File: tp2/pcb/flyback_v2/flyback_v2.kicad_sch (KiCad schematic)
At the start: 57 parts, among them J1 Connector_2, J10 Connector_2, J11 Connector_2, J2 Connector_2, J3 Connector_2, J4 Connector_2, J5 Connector_2, J6 Connector_2, J7 Terminal_2, J8 Terminal_2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

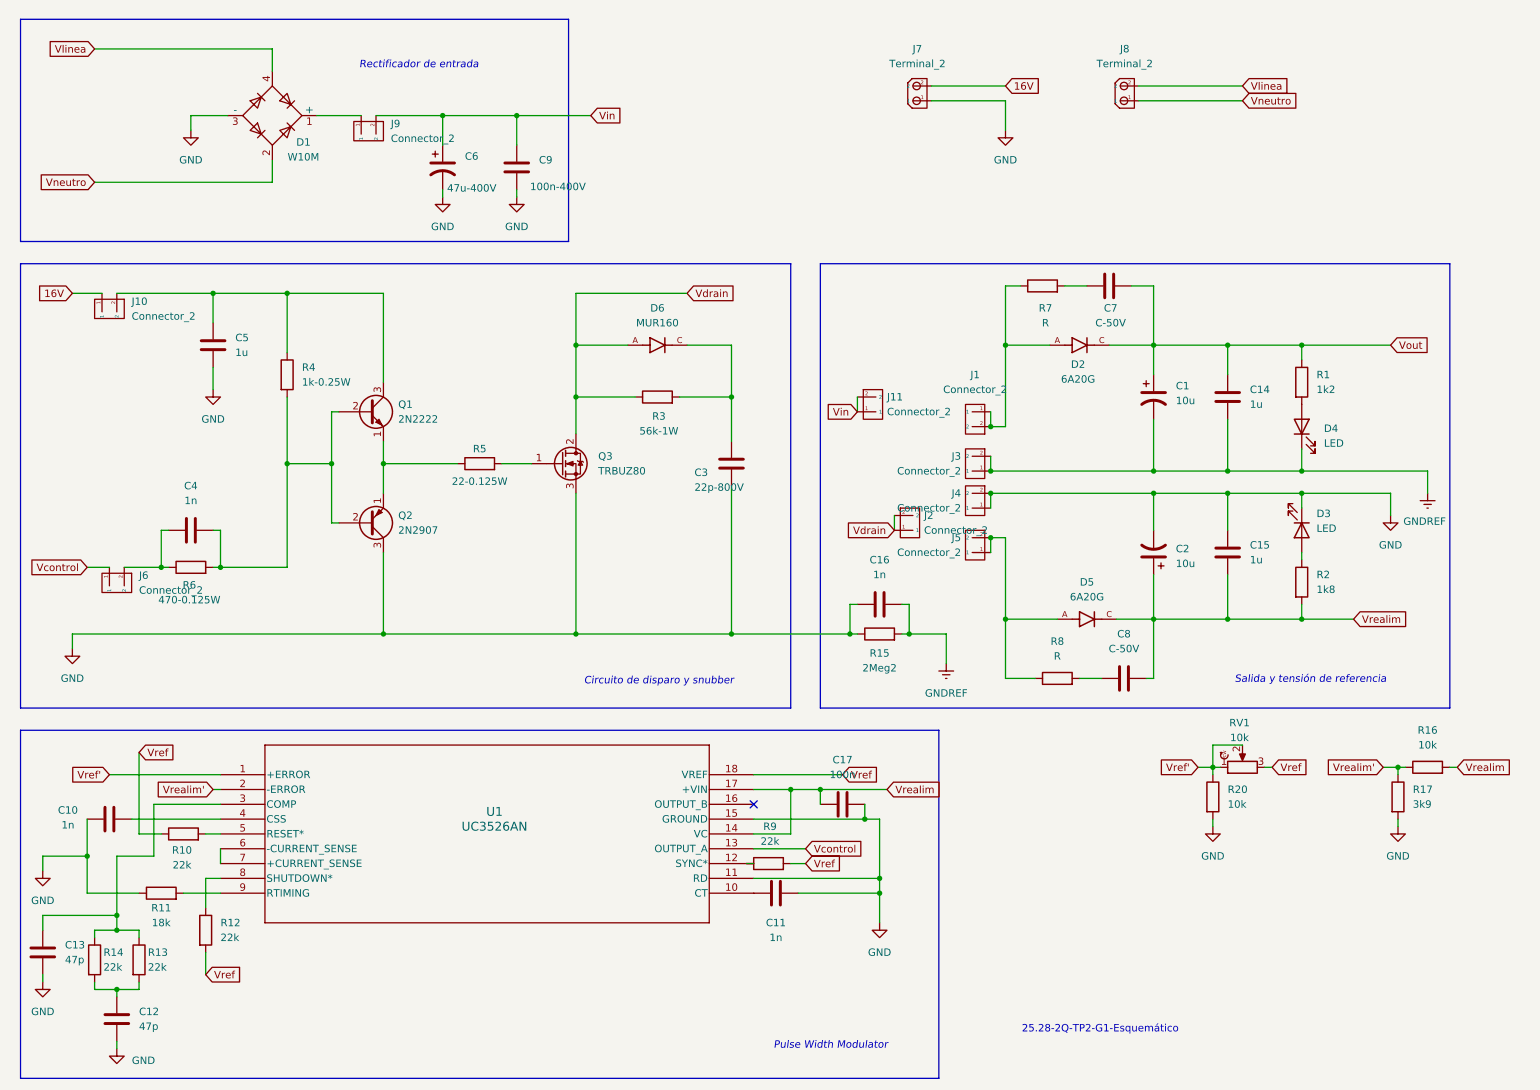
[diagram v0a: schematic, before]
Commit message: puse el jumper de Vrealim y 16V
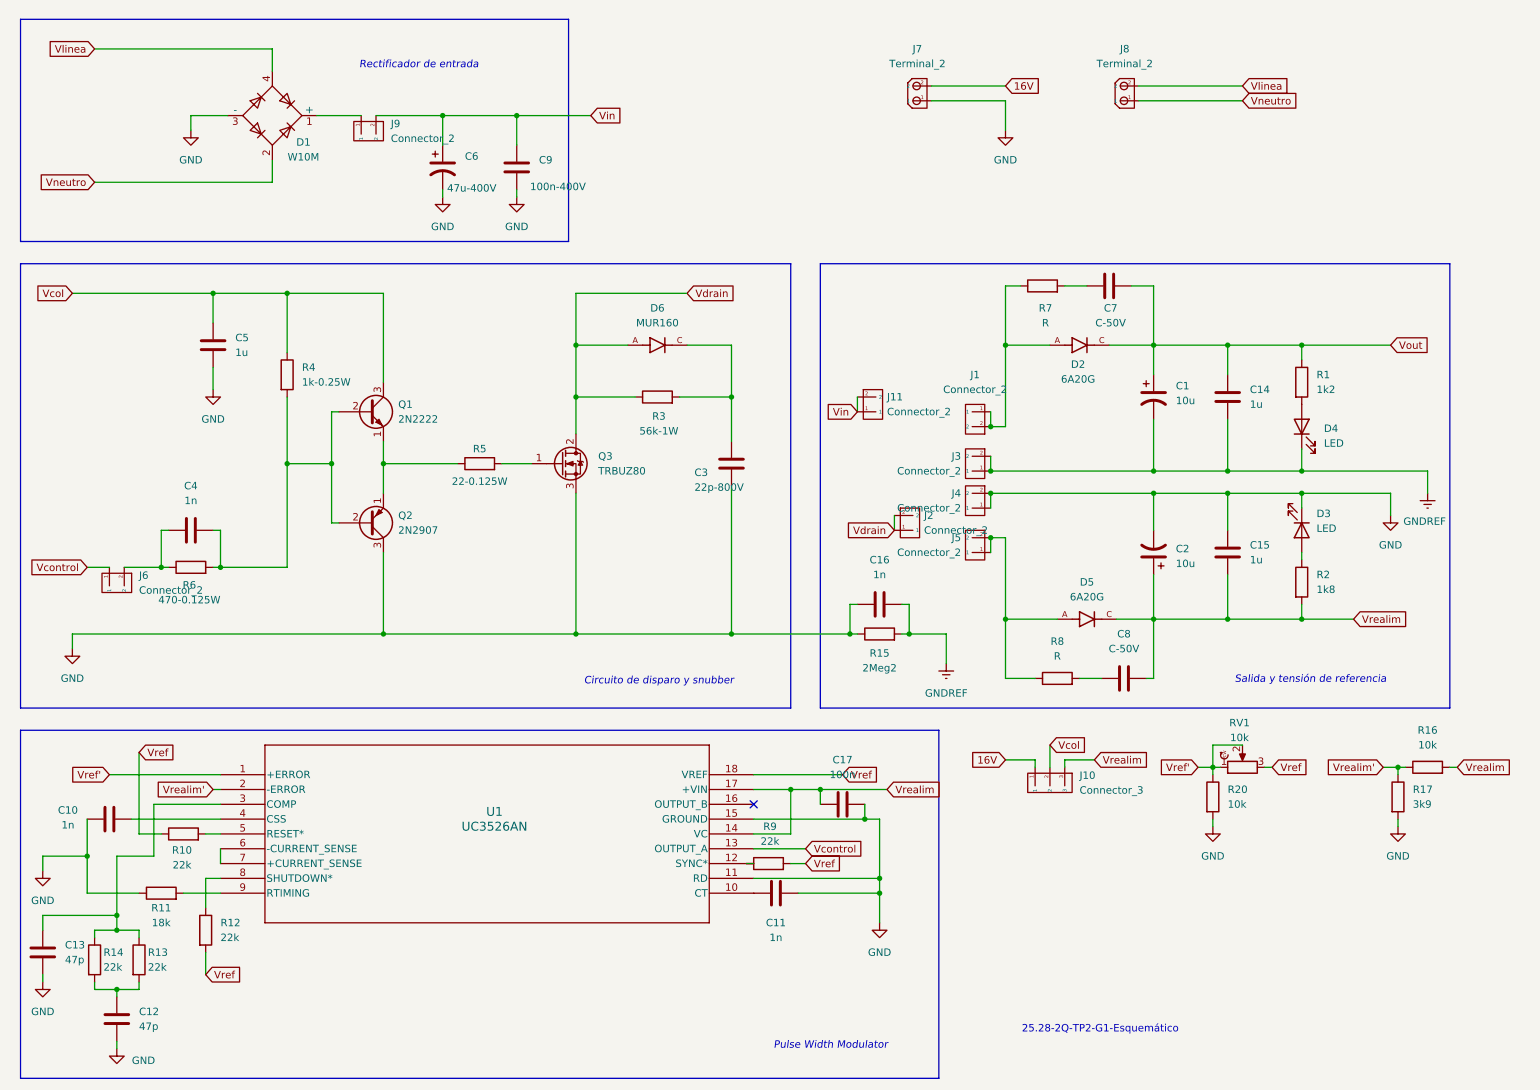
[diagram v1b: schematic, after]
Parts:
- removed J10: Connector_2, TCLib:PinHeader_1x02_P2.54mm_Vertical, symbol TCLib:Connector_2
- added J10: Connector_3, TCLib:PinHeader_1x03_P2.54mm_Vertical, symbol TCLib:Connector_3
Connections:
- net 16V: now also J10.1
- net Vrealim: now also J10.3
- net Vcol: now reaches C5.1, Q1.3 (C), R4.1
- net Vcol: now also J10.2
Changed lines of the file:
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@@
 	(wire
 		(pts
+			(xy 193.04 144.78) (xy 193.04 143.51)
+		)
+		(stroke
+			(width 0)
+			(type default)
+		)
+	)
+	(wire
+		(pts
 			(xy 187.96 105.41) (xy 187.96 119.38)
 		)
@@
 	(wire
 		(pts
+			(xy 198.12 143.51) (xy 203.2 143.51)
+		)
+		(stroke
+			(width 0)
+			(type default)
+		)
+	)
+	(wire
+		(pts
 			(xy 50.8 163.83) (xy 50.8 168.91)
 		)
@@
 	(wire
 		(pts
+			(xy 198.12 144.78) (xy 198.12 143.51)
+		)
+		(stroke
+			(width 0)
+			(type default)
+		)
+	)
+	(wire
+		(pts
 			(xy 91.44 33.02) (xy 104.14 33.02)
 		)
@@
 	(wire
 		(pts
-			(xy 35.56 63.5) (xy 52.07 63.5)
-		)
-		(stroke
-			(width 0)
-			(type default)
-		)
-	)
-	(wire
-		(pts
 			(xy 35.56 182.88) (xy 35.56 184.15)
 		)
@@
 	(wire
 		(pts
+			(xy 187.96 143.51) (xy 193.04 143.51)
+		)
+		(stroke
+			(width 0)
+			(type default)
+		)
+	)
+	(wire
+		(pts
 			(xy 252.73 144.78) (xy 255.27 144.78)
 		)
@@
 	(wire
 		(pts
+			(xy 195.58 140.97) (xy 195.58 144.78)
+		)
+		(stroke
+			(width 0)
+			(type default)
+		)
+	)
+	(wire
+		(pts
 			(xy 41.91 151.13) (xy 41.91 160.02)
 		)
@@
 	(wire
 		(pts
-			(xy 27.94 63.5) (xy 33.02 63.5)
+			(xy 27.94 63.5) (xy 52.07 63.5)
 		)
 		(stroke
@@
 		)
 	)
+	(global_label "Vrealim"
+		(shape input)
+		(at 203.2 143.51 0)
+		(fields_autoplaced yes)
+		(effects
+			(font
+				(size 1.27 1.27)
+			)
+			(justify left)
+		)
+		(property "Intersheetrefs" "${INTERSHEET_REFS}"
+			(at 213.2609 143.51 0)
+			(effects
+				(font
+					(size 1.27 1.27)
+				)
+				(justify left)
+				(hide yes)
+			)
+		)
+	)
 	(global_label "Vref"
 		(shape input)
@@
 	(global_label "16V"
 		(shape input)
+		(at 187.96 143.51 180)
+		(fields_autoplaced yes)
+		(effects
+			(font
+				(size 1.27 1.27)
+			)
+			(justify right)
+		)
+		(property "Intersheetrefs" "${INTERSHEET_REFS}"
+			(at 181.4672 143.51 0)
+			(effects
+				(font
+					(size 1.27 1.27)
+				)
+				(justify right)
+				(hide yes)
+			)
+		)
+	)
+	(global_label "16V"
+		(shape input)
 		(at 187.96 27.94 0)
 		(fields_autoplaced yes)
@@
 		)
 	)
+	(global_label "Vcol"
+		(shape input)
+		(at 195.58 140.97 0)
+		(fields_autoplaced yes)
+		(effects
+			(font
+				(size 1.27 1.27)
+			)
+			(justify left)
+		)
+		(property "Intersheetrefs" "${INTERSHEET_REFS}"
+			(at 202.5566 140.97 0)
+			(effects
+				(font
+					(size 1.27 1.27)
+				)
+				(justify left)
+				(hide yes)
+			)
+		)
+	)
 	(global_label "Vref"
 		(shape input)
@@
 		)
 	)
-	(global_label "16V"
+	(global_label "Vcol"
 		(shape input)
 		(at 27.94 63.5 180)
@@
 		)
 		(property "Intersheetrefs" "${INTERSHEET_REFS}"
-			(at 21.4472 63.5 0)
+			(at 20.9634 63.5 0)
 			(effects
 				(font
@@
 	)
 	(symbol
-		(lib_id "TCLib:Connector_2")
-		(at 34.29 66.04 270)
-		(unit 1)
-		(exclude_from_sim no)
-		(in_bom yes)
-		(on_board yes)
-		(dnp no)
-		(fields_autoplaced yes)
-		(property "Reference" "J10"
-			(at 38.1 64.8969 90)
-			(effects
-				(font
-					(size 1.27 1.27)
-				)
-				(justify left)
-			)
-		)
-		(property "Value" "Connector_2"
-			(at 38.1 67.4369 90)
-			(effects
-				(font
-					(size 1.27 1.27)
-				)
-				(justify left)
-			)
-		)
-		(property "Footprint" "TCLib:PinHeader_1x02_P2.54mm_Vertical"
-			(at 38.608 65.532 0)
-			(effects
-				(font
-					(size 1.27 1.27)
-				)
-				(hide yes)
-			)
-		)
-		(property "Datasheet" ""
-			(at 34.29 66.04 0)
-			(effects
-				(font
-					(size 1.27 1.27)
-				)
-				(hide yes)
-			)
-		)
-		(property "Description" ""
-			(at 34.29 66.04 0)
-			(effects
-				(font
-					(size 1.27 1.27)
-				)
-				(hide yes)
-			)
-		)
-		(pin "2"
-		)
-		(pin "1"
-		)
-		(instances
-			(project "flybackkoki"
-				(path "/e1bc5ebe-0245-4788-8a28-7e348d07e41a"
-					(reference "J10")
-					(unit 1)
-				)
-			)
-		)
-	)
-	(symbol
 		(lib_id "TCLib:C")
 		(at 160.02 151.13 270)
@@
 					(unit 1)
 				)
+			)
+		)
+	)
+	(symbol
+		(lib_id "TCLib:Connector_3")
+		(at 195.58 147.32 270)
+		(unit 1)
+		(exclude_from_sim no)
+		(in_bom yes)
+		(on_board yes)
+		(dnp no)
+		(fields_autoplaced yes)
+		(property "Reference" "J10"
+			(at 200.66 146.1769 90)
+			(effects
+				(font
+					(size 1.27 1.27)
+				)
+				(justify left)
+			)
+		)
+		(property "Value" "Connector_3"
+			(at 200.66 148.7169 90)
+			(effects
+				(font
+					(size 1.27 1.27)
+				)
+				(justify left)
+			)
+		)
+		(property "Footprint" "TCLib:PinHeader_1x03_P2.54mm_Vertical"
+			(at 203.708 147.574 0)
+			(effects
+				(font
+					(size 1.27 1.27)
+				)
+				(hide yes)
+			)
+		)
+		(property "Datasheet" ""
+			(at 194.31 147.32 0)
+			(effects
+				(font
+					(size 1.27 1.27)
+				)
+				(hide yes)
+			)
+		)
+		(property "Description" ""
+			(at 194.31 147.32 0)
+			(effects
+				(font
+					(size 1.27 1.27)
+				)
+				(hide yes)
+			)
+		)
+		(pin "2"
+		)
+		(pin "1"
+		)
+		(pin "3"
+		)
+		(instances
+			(project ""
+				(path "/e1bc5ebe-0245-4788-8a28-7e348d07e41a"
+					(reference "J10")
+					(unit 1)
+				)

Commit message: version final sch
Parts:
- removed C4: 1n, TCLib:C_2.5mm, symbol Device:C
- removed D2, D5: 6A20G, 6A20G:DIOAD1950W125L885D700, symbol 6A20G:6A20G
- removed R6: 470-0.125W, TCLib:R_0.125W, symbol Device:R
- added D2, D7: MUR460, MUR460:DIOAD1990W125L900D530, symbol MUR460:MUR460
- added D5: MUR160, MUR160:DIOAD1300W80L670D310, symbol MUR160:MUR160
- C3: value 22p-800V -> C_s
- R3: value 56k-1W -> R_s
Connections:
- net GND: now also U1.6 (-CURRENT_SENSE), U1.7 (+CURRENT_SENSE)
- net Vout: now also D2.C, D7.C
- net Vrealim: now also D5.C
- net at J1.1, J1.2, R7.1: now also D2.A, D7.A
- net at J6.2: now also Q1.2 (B), Q2.2 (B), R4.2
- net at J5.1, J5.2, R8.1: now also D5.A
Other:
- moved on the sheet: C16, J11, J2, J7, J8, R15
